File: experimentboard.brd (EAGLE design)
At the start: 110.5 x 100 mm, 179 parts, among them IC1 TL072P, IC2 LM317, IC3 LM337, IC4 TL072P, IC5 TL072P, IC6 TL072P, P1 PLR135/T9, P9 P9, Q1 BS170, Q2 BS170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

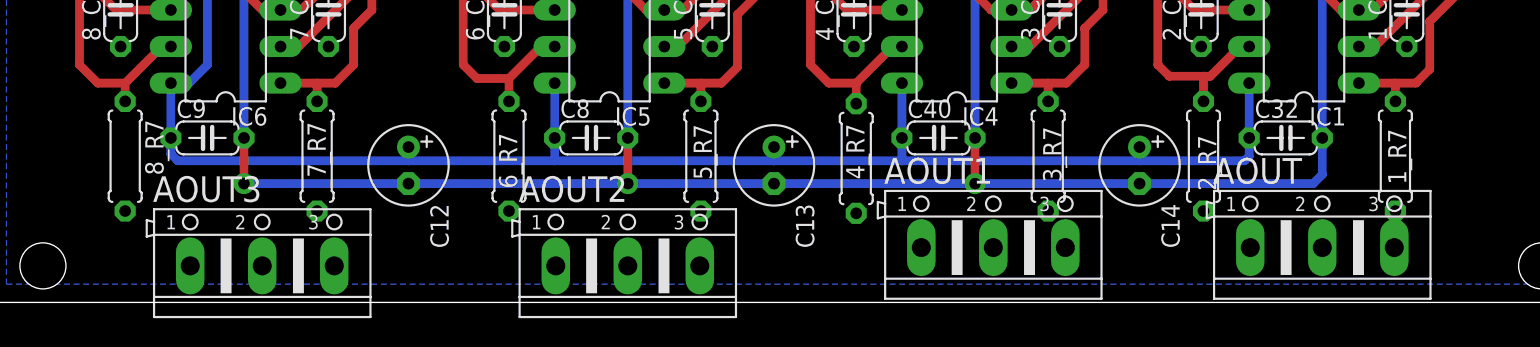
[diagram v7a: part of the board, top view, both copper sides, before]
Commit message: Molex output connectors
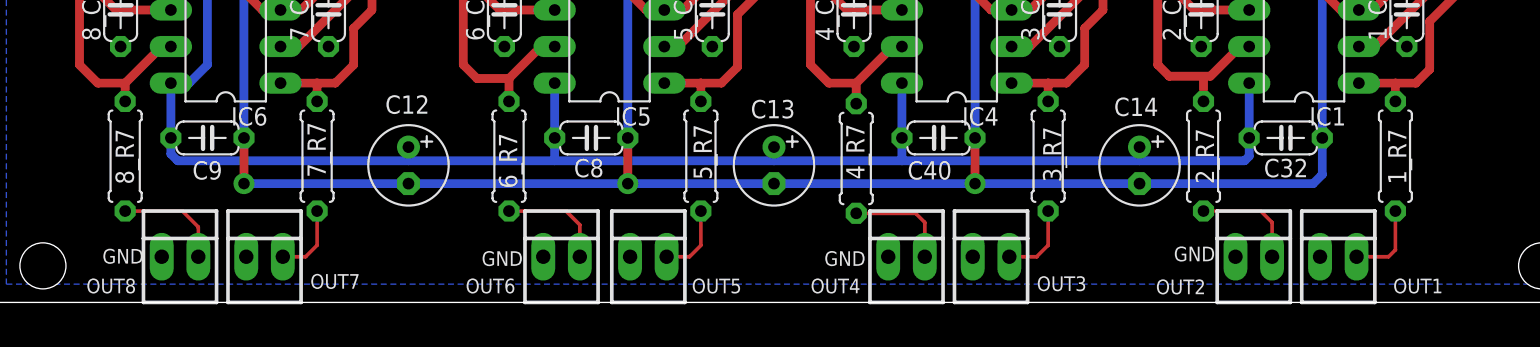
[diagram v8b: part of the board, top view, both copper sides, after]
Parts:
- removed AOUT, AOUT1, AOUT2, AOUT3: (no value), con-ptr500:AK500/3
- added OUT1, OUT2, OUT3, OUT4, OUT5, OUT6, OUT7, OUT8: 22-23-2021, con-molex:22-23-2021
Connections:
- net AGND: now also OUT1.1, OUT2.1, OUT3.1, OUT4.1, OUT5.1, OUT6.1, OUT7.1, OUT8.1; no longer AOUT.2, AOUT1.2, AOUT2.2, AOUT3.2
- net N$37: now also OUT1.2; no longer AOUT.3
- net N$38: now also OUT2.2; no longer AOUT.1
- net N$64: now also OUT3.2; no longer AOUT1.3
- net N$65: now also OUT4.2; no longer AOUT1.1
- net N$82: now also OUT5.2; no longer AOUT2.3
- net N$83: now also OUT6.2; no longer AOUT2.1
- net N$89: now also OUT7.2; no longer AOUT3.3
- net N$90: now also OUT8.2; no longer AOUT3.1
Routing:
- net N$90: track 0.00 -> 7.60 mm
- net N$83: track 0.00 -> 7.54 mm
- net N$38: track 0.00 -> 7.47 mm
- net N$65: track 0.00 -> 7.41 mm
- net N$37: track 0.00 -> 5.59 mm
- net N$64: track 0.00 -> 5.41 mm
- net N$82: track 0.00 -> 5.09 mm
- net N$89: track 0.00 -> 5.09 mm
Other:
- board text added: "GND"
